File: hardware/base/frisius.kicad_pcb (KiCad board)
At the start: 4 copper layers, 46 x 85 mm, 124 parts, among them J1 MEM2067, J2 USB_C_Receptacle_USB2.0, J3 BATTERY, J4 Debug UART, J5 Conn_02x16_Odd_Even_MountingP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, J7 I2C ISENSE, Q2 Q_NMOS_DGS, Q3 Q_NMOS_DGS, SW1 RESET, SW2 BOOT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

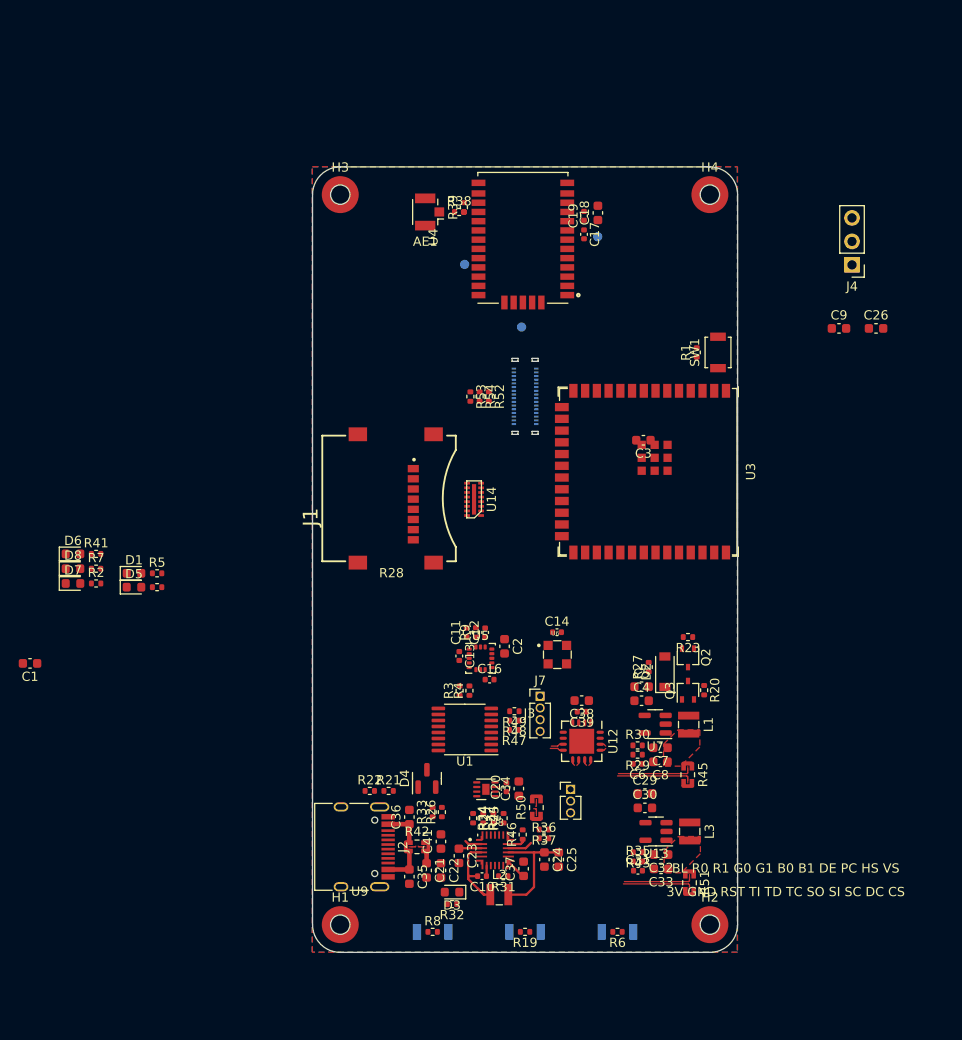
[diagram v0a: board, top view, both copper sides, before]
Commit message: completed layout for lcdboard prototype, may need to move b2b down for clearance on mainboard.
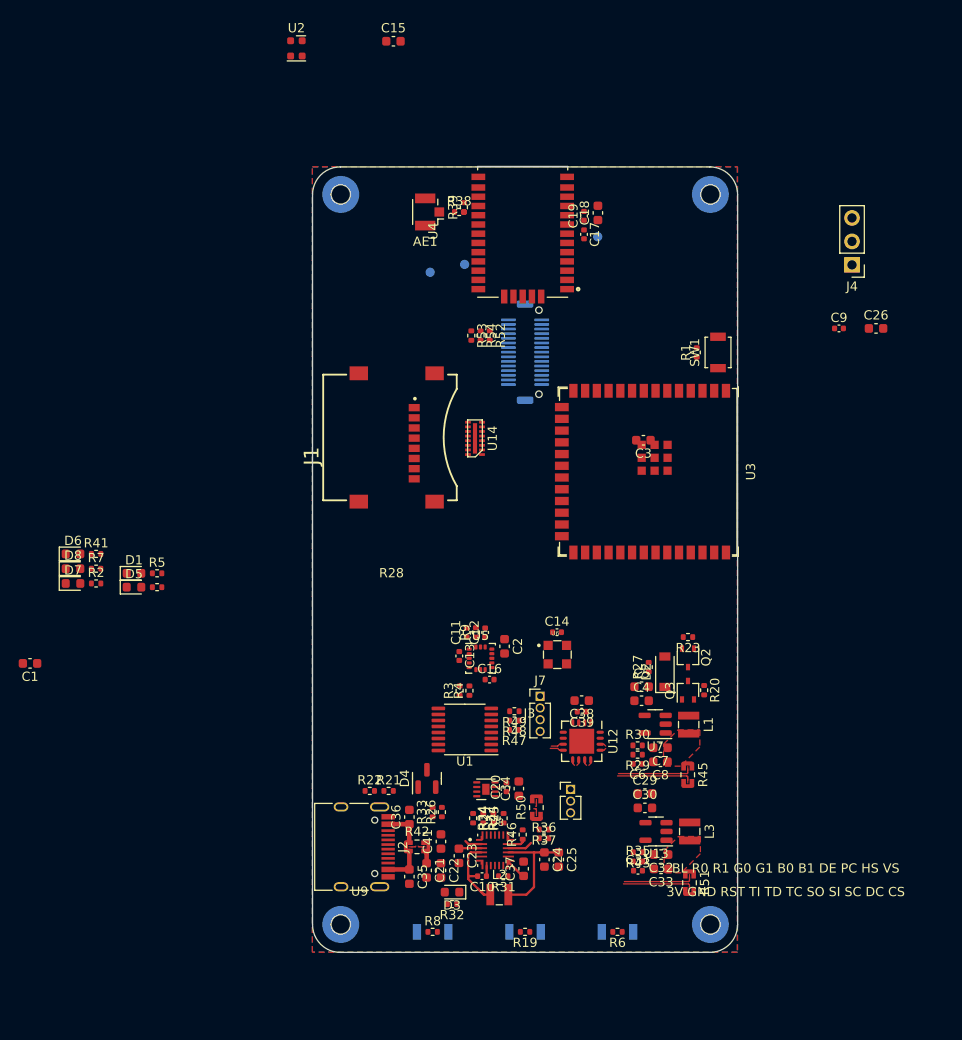
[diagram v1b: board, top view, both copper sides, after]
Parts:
- added C15: 1u, Capacitor_SMD:C_0603_1608Metric, F.Cu at (60.8, 31.4)
- added U2: LTR-329ALS-01, Package_LGA:VLGA-4_2x2.5mm_P1.65mm, F.Cu at (50.3, 32.2)
- C9: value 1u -> 0.1u; footprint Capacitor_SMD:C_0603_1608Metric -> Capacitor_SMD:C_0402_1005Metric
- H1, H2, H3, H4: moved to B.Cu
- J5: value Conn_02x16_Odd_Even_MountingPin -> Conn_02x15_Odd_Even_MountingPin; footprint Connector_Molex:Molex_SlimStack_502426-3210_2x16_P0.40mm_Vertical -> bt_Connector_B2B:10132797-031100LF
- moved H1 40.1 mm to (95.1, 127.0), turned to 180 degrees
- moved H3 40.1 mm to (95.1, 48.0), turned to 180 degrees
- moved H2 39.9 mm to (55.1, 127.0), turned to 180 degrees
- moved H4 39.9 mm to (55.1, 48.0), turned to 180 degrees
- moved TP14 11.5 mm to (64.8, 56.4)
- moved J1 6.60 mm to (60.4, 74.3)
- moved R52 6.60 mm to (71.2, 63.3)
- moved R53 6.60 mm to (69.2, 63.3)
- moved R54 6.60 mm to (70.2, 63.3)
- moved U14 6.60 mm to (69.6, 74.4)
- moved J5 4.78 mm to (75.0, 65.1), turned to 90 degrees
- moved U4 0.65 mm to (74.8, 52.0)
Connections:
- C26 pad 1: VDD_NVDC -> VDD_AUX_3V3
- J5 pad 10: /Display/LCD_RGB.B1 -> /Display/LCD_RGB.R2
- J5 pad 11: /Display/SYS_I2C.SDA -> /Display/LCD_RGB.R1
- J5 pad 12: /Display/LCD_RGB.B0 -> /Display/LCD_RGB.R0
- J5 pad 13: /Display/TOUCH_INT -> GND
- J5 pad 14: /Display/LCD_RGB.G2 -> VDD_AUX_3V3
- J5 pad 15: /Display/LCD_SPI_CS -> GND
- J5 pad 16: /Display/LCD_RGB.G1 -> GND
- J5 pad 17: /Display/LCD_MUX0 -> VDD_NVDC
- J5 pad 18: /Display/LCD_RGB.G0 -> GND
- J5 pad 19: /Display/LCD_MUX1 -> /Display/LCD_MUX3
- J5 pad 2: GND -> ~{RESET}
- J5 pad 20: /Display/LCD_RGB.R2 -> /Display/LCD_MUX2
- J5 pad 21: /Display/LCD_MUX2 -> /Display/LCD_SPI_CS
- J5 pad 22: /Display/LCD_RGB.R1 -> /Display/LCD_MUX1
- J5 pad 23: /Display/LCD_MUX3 -> /Display/LCD_MUX0
- J5 pad 24: /Display/LCD_RGB.R0 -> GND
- J5 pad 25: GND -> /Display/DISPLAY_BL
- J5 pad 27: VDD_AUX_3V3 -> /Display/TOUCH_SCL
- J5 pad 28: VDD_NVDC -> /Display/TOUCH_SDA
- J5 pad 29: VDD_AUX_3V3 -> /Display/TOUCH_INT
- J5 pad 3: ~{RESET} -> /Display/LCD_RGB.B1
- J5 pad 30: VDD_NVDC -> GND
- J5 pad 4: unconnected-(J5-Pad4) -> /Display/LCD_RGB.B0
- J5 pad 5: unconnected-(J5-Pad5) -> GND
- J5 pad 6: /Display/DISPLAY_BL -> /Display/LCD_RGB.G2
- J5 pad 7: GND -> /Display/LCD_RGB.G1
- J5 pad 8: GND -> /Display/LCD_RGB.G0
- J5 pad 9: /Display/SYS_I2C.SCL -> GND

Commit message: screen design freeze, 3d model added to base, routed display connector, sd, usb
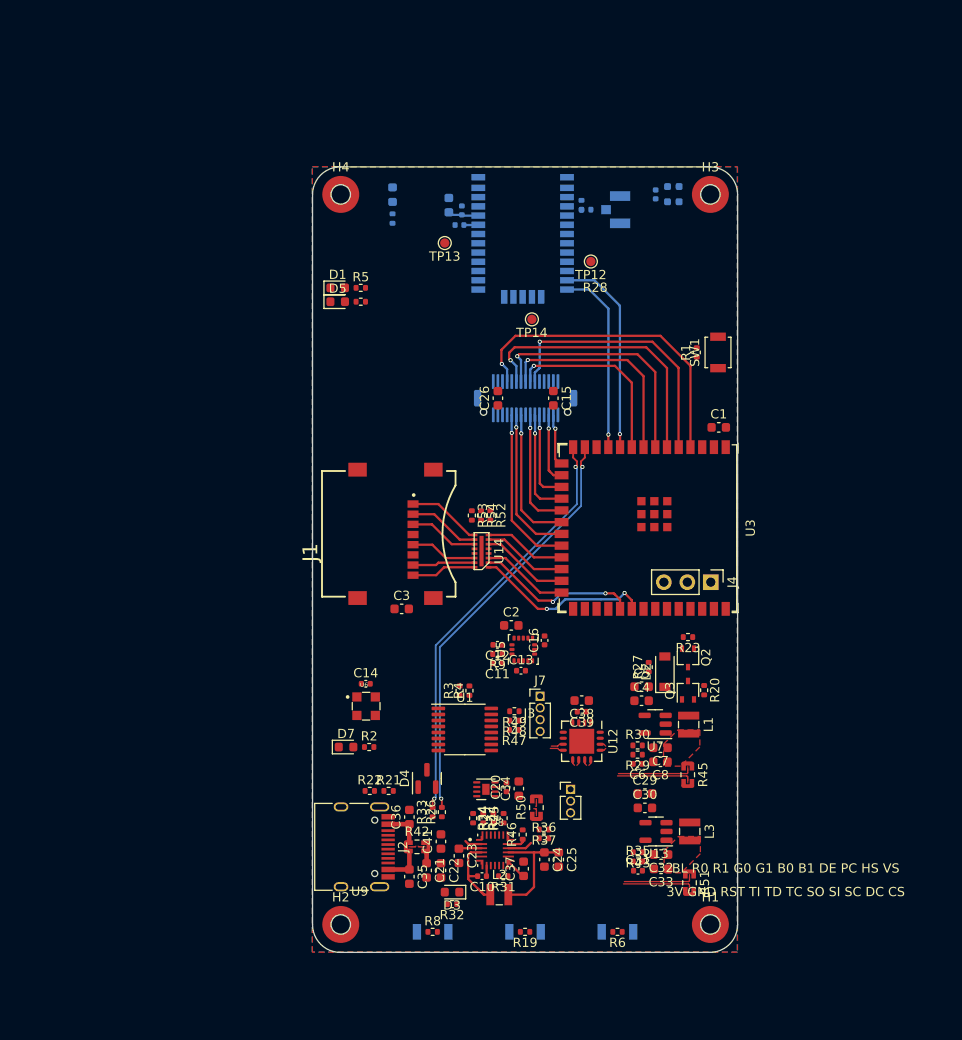
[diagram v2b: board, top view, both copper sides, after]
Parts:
- removed D8: LED_Small_Filled, LED_SMD:LED_0603_1608Metric
- removed R7: 1k, Resistor_SMD:R_0402_1005Metric
- AE1, C17, C18, C19, C9, D6, R38, R39, R41, U2, U4: moved to B.Cu
- H1, H2, H3, H4, TP12, TP13, TP14: moved to F.Cu
- J5: value Conn_02x15_Odd_Even_MountingPin -> DISPLAY
- moved C1 78.8 mm to (96.0, 73.2), turned to 0 degrees
- moved D6 52.0 mm to (60.7, 48.0), turned to -90 degrees
- moved R41 48.4 mm to (60.7, 50.6), turned to -90 degrees
- moved U2 43.7 mm to (91.1, 48.0)
- moved C15 42.3 mm to (78.1, 70.0), turned to -90 degrees
- moved C26 41.6 mm to (72.1, 70.0), turned to 90 degrees
- moved D1 37.9 mm to (54.7, 58.1)
- moved D5 37.9 mm to (54.7, 59.6)
- moved R28 37.9 mm to (57.2, 59.6)
- moved R5 37.9 mm to (57.2, 58.1)
- moved J4 37.6 mm to (95.1, 90.0), turned to -90 degrees
- moved D7 34.4 mm to (55.6, 107.8)
- moved R2 34.4 mm to (58.1, 107.8)
- moved C3 31.9 mm to (61.7, 92.8), turned to 0 degrees
- moved C9 24.6 mm to (89.2, 48.0), turned to 90 degrees
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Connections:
- C15 pad 1: VDD_NVDC -> VDD_AUX_3V3
- J4 pad 2: /Processor/DEBUG_RX -> /Processor/DEBUG_TX
- J4 pad 3: /Processor/DEBUG_TX -> /Processor/DEBUG_RX
- J5 pad 10: /Display/LCD_RGB.R2 -> /Display/LCD_RGB.R1
- J5 pad 11: /Display/LCD_RGB.R1 -> /Display/LCD_RGB.R0
- J5 pad 12: /Display/LCD_RGB.R0 -> GND
- J5 pad 13: GND -> VDD_AUX_3V3
- J5 pad 16: GND -> unconnected-(J5-Pad16)
- J5 pad 17: VDD_NVDC -> /Display/SYS_I2C.SCL
- J5 pad 18: GND -> /Display/SYS_I2C.SDA
- J5 pad 19: /Display/LCD_MUX3 -> /Display/TOUCH_INT
- J5 pad 2: ~{RESET} -> /Display/LCD_RGB.B1
- J5 pad 20: /Display/LCD_MUX2 -> /Display/DISPLAY_BL
- J5 pad 21: /Display/LCD_SPI_CS -> /Display/LCD_MUX0
- J5 pad 23: /Display/LCD_MUX0 -> /Display/LCD_MUX2
- J5 pad 24: GND -> /Display/LCD_MUX3
- J5 pad 25: /Display/DISPLAY_BL -> /Display/LCD_SPI_CS
- J5 pad 26: GND -> ~{RESET}
- J5 pad 27: /Display/TOUCH_SCL -> GND
- J5 pad 28: /Display/TOUCH_SDA -> VDD_AUX_3V3
- J5 pad 29: /Display/TOUCH_INT -> VDD_AUX_3V3
- J5 pad 3: /Display/LCD_RGB.B1 -> /Display/LCD_RGB.B0
- J5 pad 4: /Display/LCD_RGB.B0 -> GND
- J5 pad 5: GND -> /Display/LCD_RGB.G2
- J5 pad 6: /Display/LCD_RGB.G2 -> /Display/LCD_RGB.G1
- J5 pad 7: /Display/LCD_RGB.G1 -> /Display/LCD_RGB.G0
- J5 pad 8: /Display/LCD_RGB.G0 -> GND
- J5 pad 9: GND -> /Display/LCD_RGB.R2
- U3 pad 15: /Display/LCD_RGB.R0 -> /Display/LCD_RGB.B1
- U3 pad 16: /Display/LCD_RGB.R1 -> /Display/LCD_RGB.B0
- U3 pad 17: /Display/LCD_RGB.R2 -> /Display/LCD_RGB.G2
- U3 pad 18: /Display/LCD_RGB.G0 -> /Display/LCD_RGB.G1
- U3 pad 19: /Display/LCD_RGB.G1 -> /Display/LCD_RGB.G0
- U3 pad 20: /Display/LCD_RGB.G2 -> /Display/LCD_RGB.R2
- U3 pad 21: /Display/LCD_RGB.B0 -> /Display/LCD_RGB.R1
- U3 pad 22: /Display/LCD_RGB.B1 -> /Display/LCD_RGB.R0
- U3 pad 23: /Display/LCD_MUX0 -> /Processor/SDMMC.D3
- U3 pad 24: /Display/LCD_MUX1 -> /Processor/SDMMC.D2
- U3 pad 25: /Display/LCD_MUX2 -> /Processor/SDMMC.CMD
- U3 pad 26: /Display/LCD_MUX3 -> /Processor/SDMMC.CLK
- U3 pad 31: /Display/LCD_SPI_CS -> /Processor/SDMMC.D0
- U3 pad 32: /Display/SYS_I2C.SCL -> /Processor/SDMMC.D1
- U3 pad 33: /Display/SYS_I2C.SDA -> /Display/SYS_I2C.SCL
- U3 pad 34: /Processor/IOEXP_INT -> /Display/SYS_I2C.SDA
- U3 pad 35: /Display/TOUCH_INT -> /Processor/IOEXP_INT
- U3 pad 4: /Processor/SDMMC.D3 -> /Display/TOUCH_INT
- U3 pad 5: /Processor/SDMMC.D2 -> /Display/LCD_SPI_CS
- U3 pad 6: /Processor/SDMMC.CMD -> /Display/LCD_MUX0
- U3 pad 7: /Processor/SDMMC.CLK -> /Display/LCD_MUX1
- U3 pad 8: /Processor/SDMMC.D0 -> /Display/LCD_MUX2
- U3 pad 9: /Processor/SDMMC.D1 -> /Display/LCD_MUX3
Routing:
- net /Power/USB_ESP.D+: track 0.00 -> 45.7 mm, vias 0 -> 2
- net /Power/USB_ESP.D-: track 0.00 -> 45.7 mm, vias 0 -> 2
- net /Display/TOUCH_INT: track 0.00 -> 34.9 mm, vias 0 -> 1
- net /Display/LCD_MUX0: track 0.00 -> 30.3 mm, vias 0 -> 1
- net /Display/LCD_SPI_CS: track 0.00 -> 29.4 mm, vias 0 -> 1
- net /Display/LCD_MUX1: track 0.00 -> 26.9 mm, vias 0 -> 1
- net /Display/LCD_MUX2: track 0.00 -> 23.4 mm, vias 0 -> 1
- net /GPS/GPS_UART.RX: track 0.00 -> 22.2 mm, vias 0 -> 1
- net /GPS/GPS_UART.TX: track 0.00 -> 20.3 mm, vias 0 -> 1
- net /Display/LCD_MUX3: track 0.00 -> 20.2 mm, vias 0 -> 1
- net /Processor/SDMMC.D1: track 0.00 -> 19.3 mm, vias 0 -> 2
- net /Display/LCD_RGB.R0: track 0.00 -> 18.0 mm, vias 0 -> 1
- net /Processor/SDMMC.D0: track 0.00 -> 17.7 mm, vias 0 -> 2
- net /Display/LCD_RGB.R1: track 0.00 -> 16.5 mm, vias 0 -> 1
- net /Display/LCD_RGB.R2: track 0.00 -> 15.2 mm, vias 0 -> 1
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
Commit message: layout
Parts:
- removed TP12: GPS_RST, TestPoint:TestPoint_Pad_D1.0mm
- removed TP13: GPS_INT, TestPoint:TestPoint_Pad_D1.0mm
- added TP1: GPS_FON, TestPoint:TestPoint_Pad_D1.0mm, F.Cu at (65.4, 56.4)
- moved R51 41.9 mm to (57.3, 100.3), turned to 90 degrees
- moved L3 37.3 mm to (57.2, 105.9), turned to 90 degrees
- moved C33 35.1 mm to (60.3, 101.8), turned to 0 degrees
- moved C32 33.5 mm to (60.3, 103.4), turned to 0 degrees
- moved C13 32.1 mm to (43.1, 106.1)
- moved C11 31.7 mm to (41.0, 105.3)
- moved C12 31.7 mm to (41.0, 103.3)
- moved C2 31.7 mm to (42.5, 101.2)
- moved R9 31.7 mm to (41.0, 104.3)
- moved U5 31.7 mm to (43.8, 103.8)
- moved C16 31.7 mm to (46.1, 102.8)
- moved C31 31.3 mm to (62.8, 101.6), turned to 180 degrees
- moved C9 30.6 mm to (58.6, 48.0)
- moved U2 30.6 mm to (60.5, 48.0)
- moved U13 30.4 mm to (60.9, 105.9), turned to 0 degrees
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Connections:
- net /Power/PORT_D+ renamed /Power/USB_D+
- net /Power/PORT_D- renamed /Power/USB_D-
- net Net-(C10-Pad1) renamed /Power/chg_bst
- net Net-(C10-Pad2) renamed /Power/chg_sw
- net Net-(C13-Pad1) renamed /Sensors/imu_byp
- net Net-(C23-Pad1) renamed /Power/chg_pmid
- net Net-(C31-Pad2) renamed /Power/vaux_fb
- net Net-(C37-Pad1) renamed /Power/chg_vref
- net Net-(C6-Pad2) renamed /Power/vcore_fb
- net Net-(D3-Pad1) renamed /Power/chg_stat
- net Net-(D3-Pad2) renamed /Power/chg_stat_led
- net Net-(D6-Pad2) renamed /Processor/esp_led
- net Net-(D7-Pad2) renamed /Processor/exp_led
- net Net-(J1-Pad1) renamed /SD Card/sd_d2
- net Net-(J1-Pad2) renamed /SD Card/sd_d3
- net Net-(J1-Pad3) renamed /SD Card/sd_cmd
- net Net-(J1-Pad5) renamed /SD Card/sd_clk
- net Net-(J1-Pad7) renamed /SD Card/sd_d0
- net Net-(J1-Pad8) renamed /SD Card/sd_d1
- net Net-(J2-PadA5) renamed /Power/usb_cc1
- net Net-(J2-PadB5) renamed /Power/usb_cc2
- net Net-(J3-Pad2) renamed /Power/bat_ntc
- net Net-(R31-Pad2) renamed /Power/chg_disc
- net Net-(R34-Pad1) renamed /Power/chg_ilim
- net Net-(R36-Pad1) renamed /Power/chg_ntc
- net Net-(R36-Pad2) renamed /Power/chg_vntc
- net Net-(R44-Pad1) renamed /Power/chg_otg
- net Net-(R46-Pad1) renamed /Power/chg_ce
- net Net-(R50-Pad1) renamed /Power/chg_batt
- net Net-(R52-Pad1) renamed /SD Card/cl_r1
- net Net-(R53-Pad1) renamed /SD Card/cl_r2
- net Net-(R54-Pad1) renamed /SD Card/cl_r3
- net Net-(R9-Pad1) renamed /Sensors/imu_reset
- U1 pad 10: /Power/ISENSE_INT -> /Power/AUX_REG_EN
- U1 pad 11: /Power/AUX_REG_EN -> /Power/SHUTDOWN
- U1 pad 12: /Power/SHUTDOWN -> /Power/ISENSE_INT
- U1 pad 14: /Display/SYS_I2C.SCL -> /Display/SYS_I2C.SDA
- U1 pad 15: /Display/SYS_I2C.SDA -> /Display/SYS_I2C.SCL
- U1 pad 4: /Processor/STATUS_IOEXP0 -> /GPS/GPS_FIX
- U1 pad 5: /Processor/NAV_BTN -> /GPS/GPS_FORCE_ON
- U1 pad 6: /GPS/GPS_FIX -> /Processor/STATUS_IOEXP0
- U1 pad 7: /GPS/GPS_FORCE_ON -> /Processor/NAV_BTN
- U12 pad 10: /Power/VCORE_S+ -> /Power/VBAT_S-
- U12 pad 11: /Power/VBUS_S+ -> /Power/VCORE_S+
- U12 pad 12: /Power/VBUS_S- -> /Power/VCORE_S-
- U12 pad 13: /Power/VBAT_S- -> /Power/VAUX_S+
- U12 pad 14: /Power/VBAT_S+ -> /Power/VAUX_S-
- U12 pad 7: /Power/VAUX_S- -> /Power/VBUS_S-
- U12 pad 8: /Power/VAUX_S+ -> /Power/VBUS_S+
- U12 pad 9: /Power/VCORE_S- -> /Power/VBAT_S+
- U3 pad 33: /Display/SYS_I2C.SCL -> /Display/SYS_I2C.SDA
- U3 pad 34: /Display/SYS_I2C.SDA -> /Display/SYS_I2C.SCL
- U4 pad 7: Net-(TP13-Pad1) -> /GPS/GPS_EXTINT0
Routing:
- net /Display/SYS_I2C.SDA: track 0.00 -> 27.5 mm
- net /Display/SYS_I2C.SCL: track 0.00 -> 26.3 mm
- net /Power/VCORE_S-: track 8.76 -> 0.00 mm
- net /Power/VCORE_S+: track 8.67 -> 0.00 mm
- net /Power/VAUX_S-: track 9.00 -> 1.32 mm
- net /Power/VAUX_S+: track 9.00 -> 1.59 mm
- net /Power/ISENSE_SCL: track 0.00 -> 6.44 mm
- net /Power/ISENSE_SDA: track 0.00 -> 4.76 mm
- net /Processor/SDMMC.D0: track 17.7 -> 15.5 mm
- net /Processor/SDMMC.D1: track 19.3 -> 17.4 mm
- net /Processor/SDMMC.CMD: track 9.54 -> 7.81 mm
- net /Processor/SDMMC.CLK: track 9.45 -> 7.71 mm
- net /Power/VBAT_S-: track 1.46 -> 0.00 mm
- net /Processor/SDMMC.D2: track 9.22 -> 7.94 mm
- net /Power/VBUS_S-: track 1.24 -> 0.00 mm
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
